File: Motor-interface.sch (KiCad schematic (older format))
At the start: 39 parts, among them J101 0, J102 0, P101 TE-23pins connector, P102 PSU_ISO, P103 Halls, P104 LineContactor, P105 ReverseContactor, P106 FanContactor, P107 Battery+, P108 MC_USB, P109 MC_CAN, Q101 Q_NPN_BCE, U101 AP1117D50, U102 AP1117D33, U103 TLP2361, U104 TLP2361, U105 TLP2361, U106 TLP2361, U107 TLP2361, U108 TLP2361, U109 Teensy_3.2, U110 TLP2361, U111 FODM3052

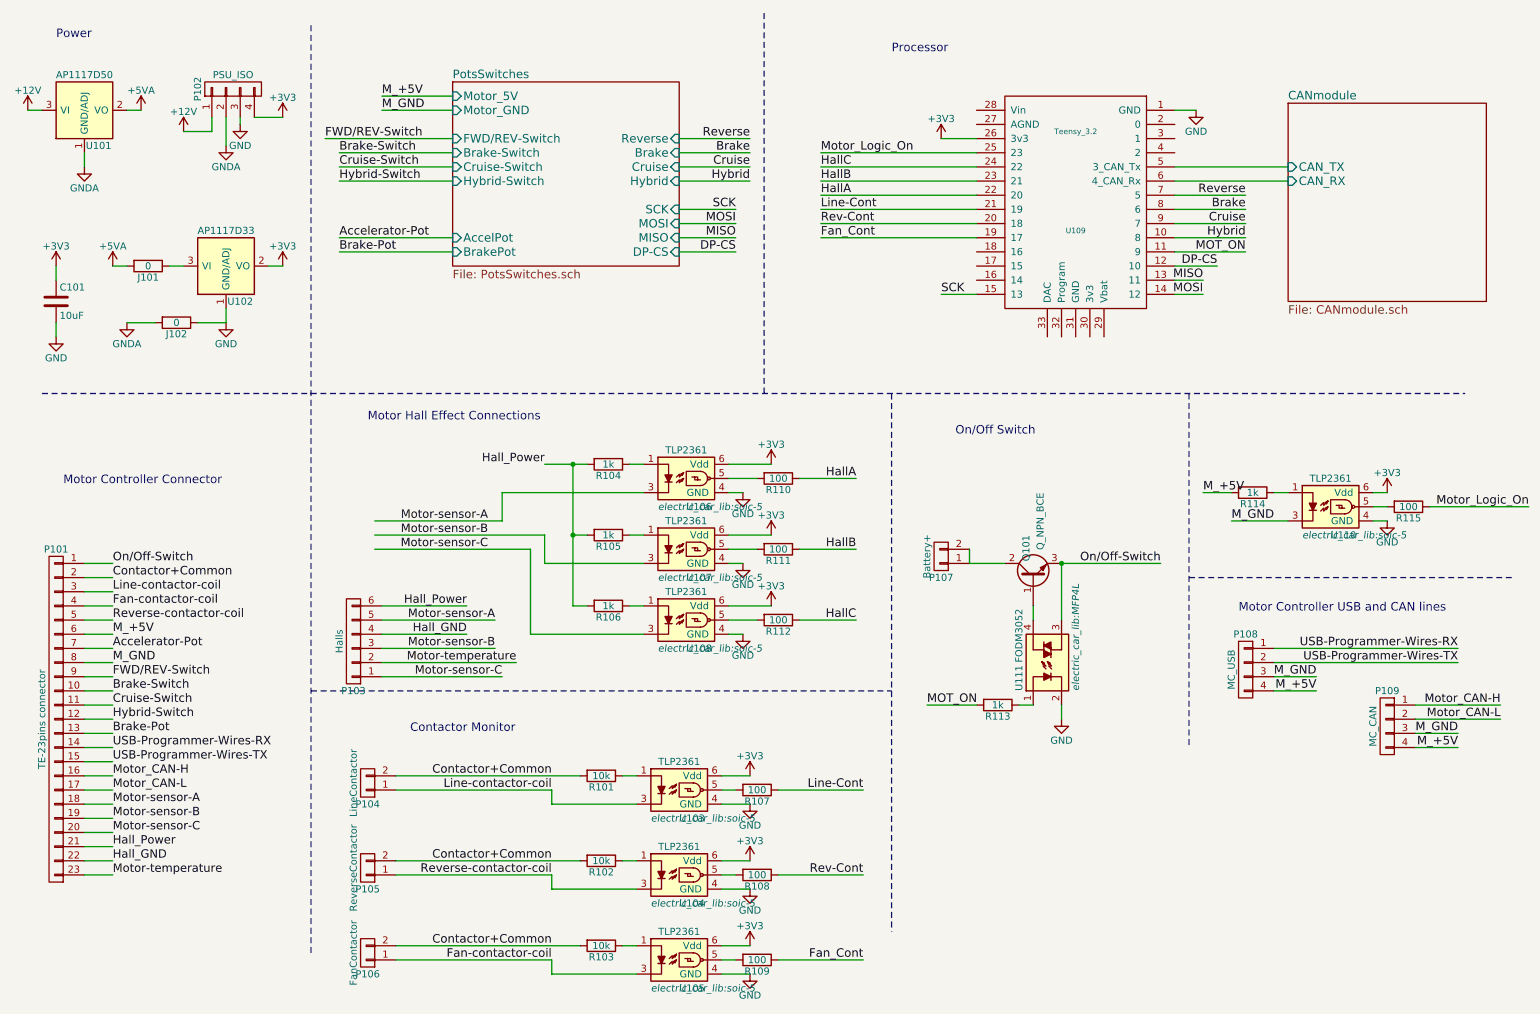
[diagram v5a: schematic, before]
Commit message: laid out Contactors and monitors
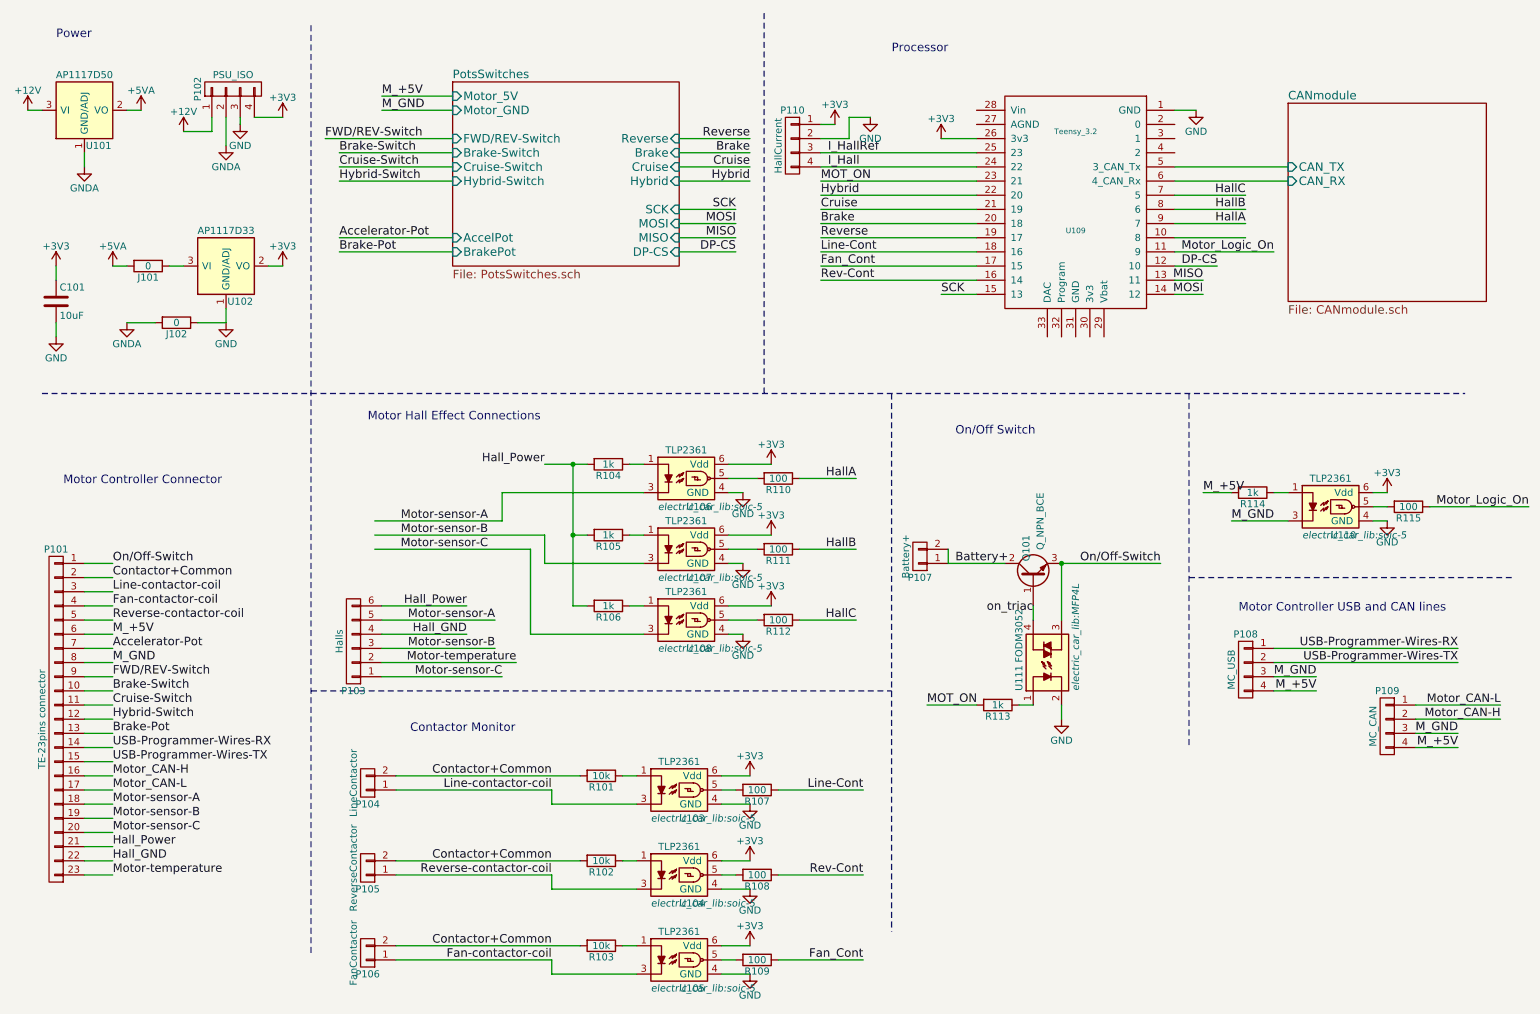
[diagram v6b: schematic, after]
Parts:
- added P110: HallCurrent, Pin_Headers:Pin_Header_Straight_1x04, symbol CONN_01X04
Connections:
- net +3V3: now also P110.1 (P1)
- net Brake: now also U109.20 (18); no longer U109.8 (6)
- net Cruise: now also U109.21 (19); no longer U109.9 (7)
- net Fan_Cont: now also U109.17 (15); no longer U109.19 (17)
- net GND: now also P110.2 (P2)
- net HallA: now also U109.9 (7); no longer U109.22 (20)
- net HallB: now also U109.8 (6); no longer U109.23 (21)
- net HallC: now also U109.7 (5); no longer U109.24 (22)
- net Hybrid: now also U109.22 (20); no longer U109.10 (8)
- net Line-Cont: now also U109.18 (16); no longer U109.21 (19)
- net MOT_ON: now also U109.23 (21); no longer U109.11 (9)
- net Motor_CAN-H: now also P109.2 (P2); no longer P109.1 (P1)
- net Motor_CAN-L: now also P109.1 (P1); no longer P109.2 (P2)
- net Motor_Logic_On: now also U109.11 (9); no longer U109.25 (23)
- net Rev-Cont: now also U109.16 (14); no longer U109.20 (18)
- net Reverse: now also U109.19 (17); no longer U109.7 (5)
- net on_triac: now reaches Q101.1 (B), U111.4
- net Battery+: now reaches P107.1 (P1), P107.2 (P2), Q101.2 (C)
- new net I_Hall: P110.4 (P4), U109.24 (22)
- new net I_HallRef: P110.3 (P3), U109.25 (23)
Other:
- moved on the sheet: P107
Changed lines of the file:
@@
 Text Label 6950 5400 0    60   ~ 0
 MOT_ON
-Text Label 9200 2200 2    60   ~ 0
+Text Label 6200 1700 0    60   ~ 0
 MOT_ON
 $Comp
@@
 Text Notes 9150 4750 0    60   ~ 0
 Motor Controller USB and CAN lines
-Text Label 9200 1800 2    60   ~ 0
+Text Label 6200 2100 0    60   ~ 0
 Reverse
 $Comp
@@
 Text Label 10700 5100 2    59   ~ 0
 USB-Programmer-Wires-TX
+Text Label 11000 5500 2    59   ~ 0
+Motor_CAN-H
 Text Label 11000 5400 2    59   ~ 0
-Motor_CAN-H
-Text Label 11000 5500 2    59   ~ 0
 Motor_CAN-L
 $Comp
@@
 	0    1    1    0
 $EndComp
-Text Label 9200 1900 2    60   ~ 0
+Text Label 6200 2000 0    60   ~ 0
 Brake
-Text Label 9200 2000 2    60   ~ 0
+Text Label 6200 1900 0    60   ~ 0
 Cruise
-Text Label 9200 2100 2    60   ~ 0
+Text Label 6200 1800 0    60   ~ 0
 Hybrid
-Text Label 6200 1900 0    60   ~ 0
+Text Label 6200 2200 0    60   ~ 0
 Line-Cont
-Text Label 6200 2000 0    60   ~ 0
+Text Label 6200 2400 0    60   ~ 0
 Rev-Cont
-Text Label 6200 2100 0    60   ~ 0
+Text Label 6200 2300 0    60   ~ 0
 Fan_Cont
 Text Label 9700 5200 2    60   ~ 0
@@
 	8700 1200 8850 1200
 Wire Wire Line
-	6200 1500 7300 1500
-Wire Wire Line
-	6200 1600 7300 1600
-Wire Wire Line
 	6200 1700 7300 1700
 Wire Wire Line
 	6200 1800 7300 1800
 Wire Wire Line
+	6200 1900 7300 1900
+Wire Wire Line
+	6200 2000 7300 2000
+Wire Wire Line
 	5600 1900 5200 1900
 Wire Wire Line
@@
 	8700 2100 9200 2100
 Wire Wire Line
-	6200 1900 7300 1900
-Wire Wire Line
-	7300 2000 6200 2000
-Wire Wire Line
 	6200 2100 7300 2100
+Wire Wire Line
+	7300 2200 6200 2200
+Wire Wire Line
+	6200 2300 7300 2300
 Wire Wire Line
 	3050 4300 4150 4300
@@
 Wire Wire Line
 	11200 4000 10500 4000
-Text Label 6200 1500 0    60   ~ 0
+Text Label 9400 2200 2    60   ~ 0
 Motor_Logic_On
-Text Label 6200 1600 0    60   ~ 0
+Text Label 9200 1800 2    60   ~ 0
 HallC
-Text Label 6200 1700 0    60   ~ 0
+Text Label 9200 1900 2    60   ~ 0
 HallB
-Text Label 6200 1800 0    60   ~ 0
+Text Label 9200 2000 2    60   ~ 0
 HallA
 Wire Wire Line
-	9200 2200 8700 2200
+	9400 2200 8700 2200
 $Comp
 L +12V #PWR018
@@
 $EndComp
 Wire Wire Line
-	7250 4400 7500 4400
+	7100 4400 7500 4400
 $Comp
 L CONN_01X02 P107
 U 1 1 582C2C61
-P 7050 4350
-F 0 "P107" H 7050 4500 50  0000 C CNN
-F 1 "Battery+" V 7150 4350 50  0000 C CNN
-F 2 "Connect:bornier2" H 7050 4350 50  0001 C CNN
-F 3 "" H 7050 4350 50  0000 C CNN
-	1    7050 4350
+P 6900 4350
+F 0 "P107" H 6900 4500 50  0000 C CNN
+F 1 "Battery+" V 7000 4350 50  0000 C CNN
+F 2 "Connect:bornier2" H 6900 4350 50  0001 C CNN
+F 3 "" H 6900 4350 50  0000 C CNN
+	1    6900 4350
 	-1   0    0    1
 $EndComp
 Wire Wire Line
-	7250 4300 7250 4400
+	7100 4300 7100 4400
 Text Label 3900 4800 2    59   ~ 0
 Motor-sensor-A
@@
 Wire Wire Line
 	3100 5200 3950 5200
+Text Label 7150 4400 0    60   ~ 0
+Battery+
+Text Label 7700 4750 2    60   ~ 0
+on_triac
+$Comp
+L CONN_01X04 P110
+U 1 1 582D9085
+P 6000 1450
+F 0 "P110" H 6000 1700 50  0000 C CNN
+F 1 "HallCurrent" V 6100 1450 50  0000 C CNN
+F 2 "Pin_Headers:Pin_Header_Straight_1x04" H 6000 1450 50  0001 C CNN
+F 3 "" H 6000 1450 50  0000 C CNN
+	1    6000 1450
+	-1   0    0    -1
+$EndComp
+$Comp
+L +3V3 #PWR031
+U 1 1 582D980D
+P 6300 1300
+F 0 "#PWR031" H 6300 1150 50  0001 C CNN
+F 1 "+3V3" H 6300 1440 50  0000 C CNN
+F 2 "" H 6300 1300 50  0000 C CNN
+F 3 "" H 6300 1300 50  0000 C CNN
+	1    6300 1300
+	1    0    0    -1
+$EndComp
+$Comp
+L GND #PWR032
+U 1 1 582D98FC
+P 6550 1250
+F 0 "#PWR032" H 6550 1000 50  0001 C CNN
+F 1 "GND" H 6550 1100 50  0000 C CNN
+F 2 "" H 6550 1250 50  0000 C CNN
+F 3 "" H 6550 1250 50  0000 C CNN
+	1    6550 1250
+	1    0    0    -1
+$EndComp
+Wire Wire Line
+	6300 1300 6200 1300
+Wire Wire Line
+	6200 1400 6400 1400
+Wire Wire Line
+	6400 1400 6400 1250
+Wire Wire Line
+	6400 1250 6550 1250
+Wire Wire Line
+	6200 1500 7300 1500
+Wire Wire Line
+	6200 1600 7300 1600
+Text Label 6250 1500 0    60   ~ 0
+I_HallRef
+Text Label 6250 1600 0    60   ~ 0
+I_Hall
+Wire Wire Line
+	7300 2400 6200 2400
 $EndSCHEMATC

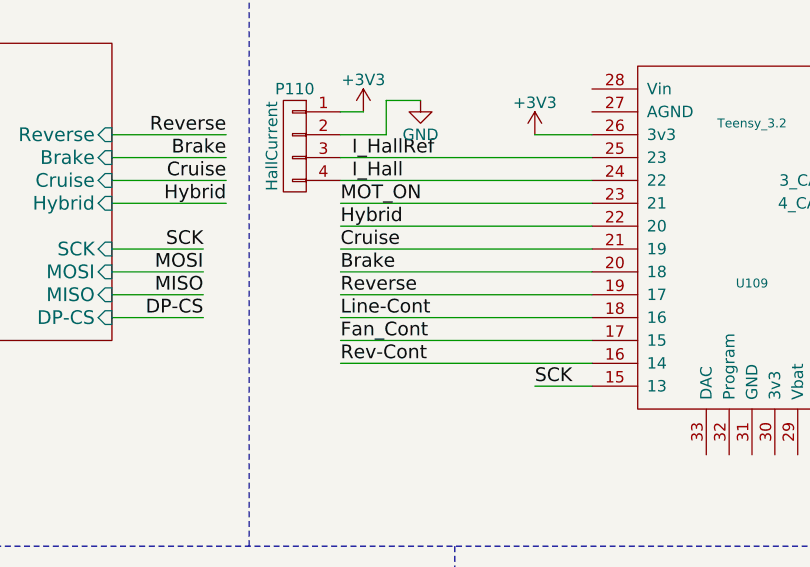
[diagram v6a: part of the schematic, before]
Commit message: laid out Contactors and monitors
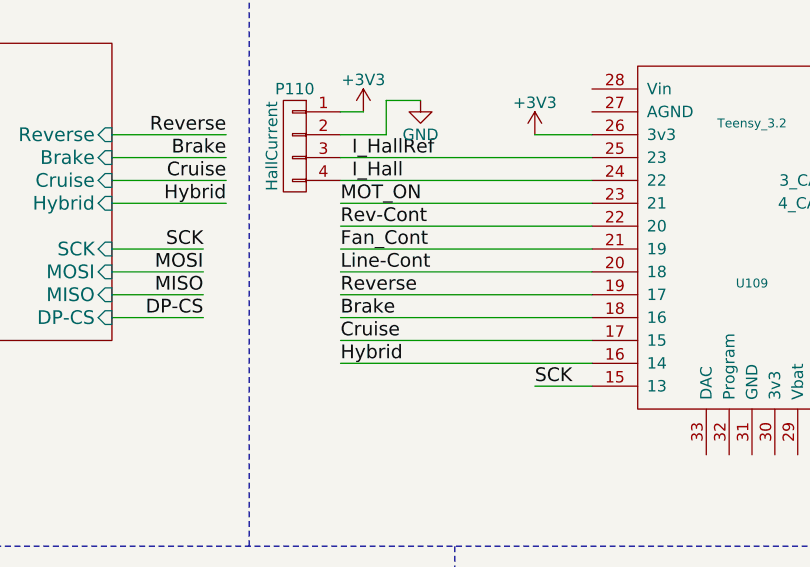
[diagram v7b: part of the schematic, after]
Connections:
- net Brake: now also U109.18 (16); no longer U109.20 (18)
- net Cruise: now also U109.17 (15); no longer U109.21 (19)
- net Fan_Cont: now also U109.21 (19); no longer U109.17 (15)
- net Hybrid: now also U109.16 (14); no longer U109.22 (20)
- net Line-Cont: now also U109.20 (18); no longer U109.18 (16)
- net Rev-Cont: now also U109.22 (20); no longer U109.16 (14)
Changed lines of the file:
@@
 	0    1    1    0
 $EndComp
+Text Label 6200 2200 0    60   ~ 0
+Brake
+Text Label 6200 2300 0    60   ~ 0
+Cruise
+Text Label 6200 2400 0    60   ~ 0
+Hybrid
 Text Label 6200 2000 0    60   ~ 0
-Brake
+Line-Cont
+Text Label 6200 1800 0    60   ~ 0
+Rev-Cont
 Text Label 6200 1900 0    60   ~ 0
-Cruise
-Text Label 6200 1800 0    60   ~ 0
-Hybrid
-Text Label 6200 2200 0    60   ~ 0
-Line-Cont
-Text Label 6200 2400 0    60   ~ 0
-Rev-Cont
-Text Label 6200 2300 0    60   ~ 0
 Fan_Cont
 Text Label 9700 5200 2    60   ~ 0
